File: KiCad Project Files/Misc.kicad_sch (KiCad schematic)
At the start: 26 parts, among them J1 EZMate, U5 SN74AHCT1G125

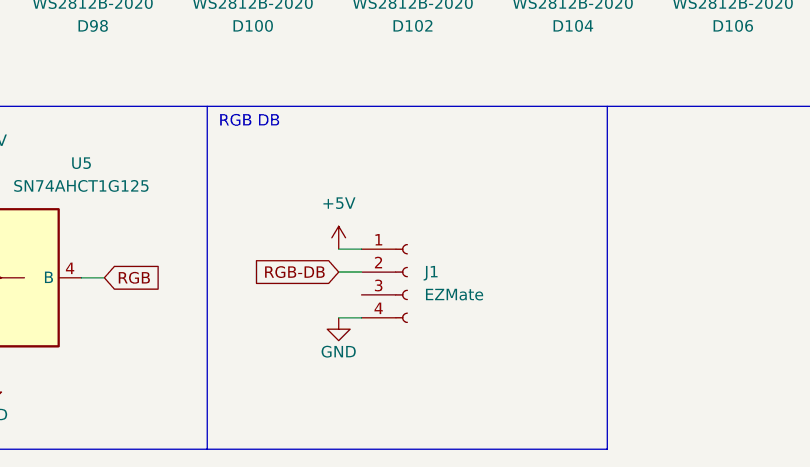
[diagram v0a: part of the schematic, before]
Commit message: added 225/275 support
2.75 stabs have break-away screw holes for compatibility with cases that need those areas of the PCB to be cut away
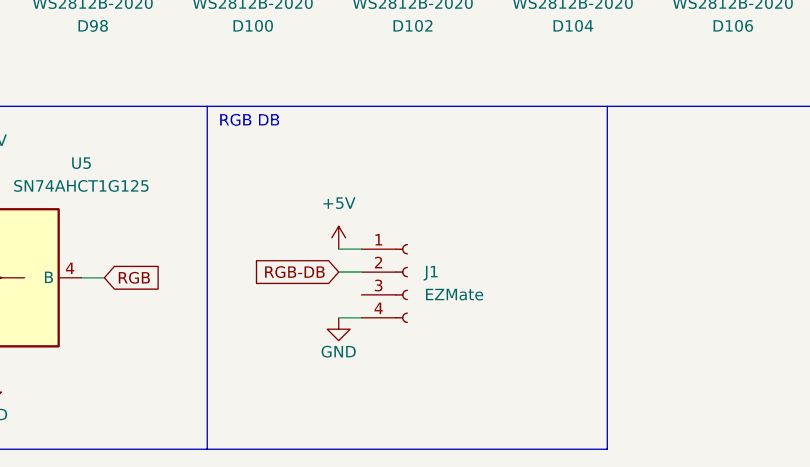
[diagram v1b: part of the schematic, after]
